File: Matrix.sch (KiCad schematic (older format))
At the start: 178 parts

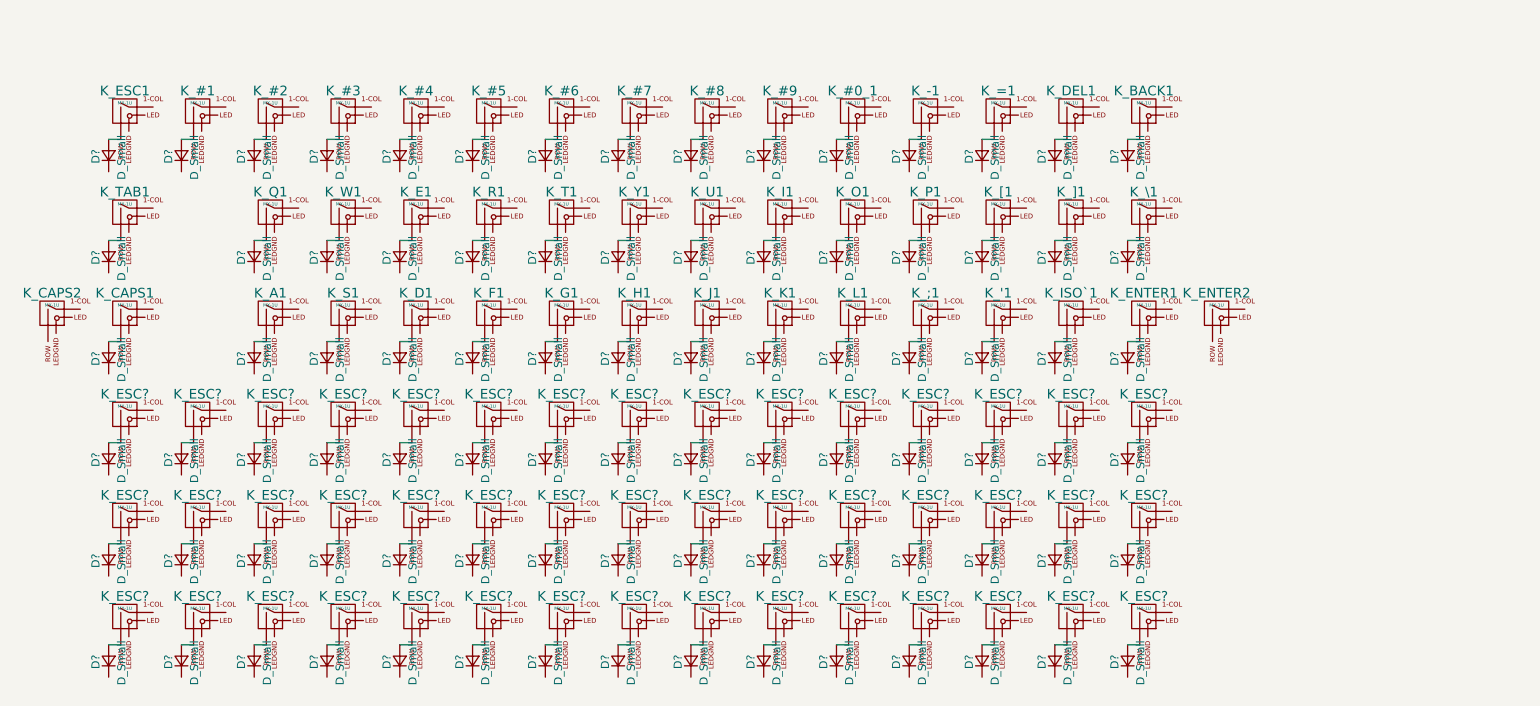
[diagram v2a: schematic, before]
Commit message: Build right shift in separate sheet
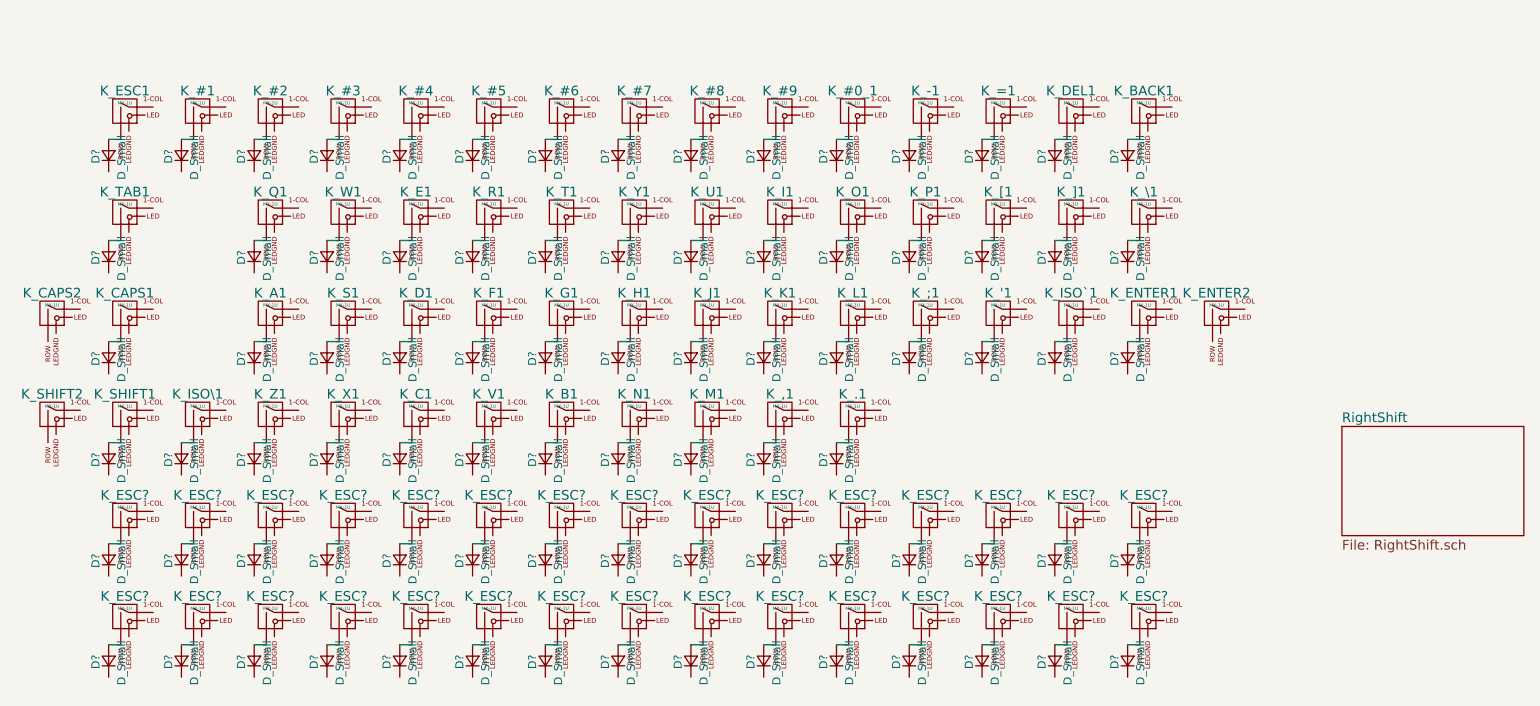
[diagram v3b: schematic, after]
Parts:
- removed D? (x34): D_Small, symbol D_Small
- removed K_ESC? (x34): MX-1U, symbol MX-1U
- added D? (x30): D_Small, symbol D_Small
- added K_ESC? (x30), K_SHIFT2: MX-1U, symbol MX-1U
- gave numbers to parts that had none: 11
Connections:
- new net: D?.2 (A), K_ESC?.2 (ROW) (x30)

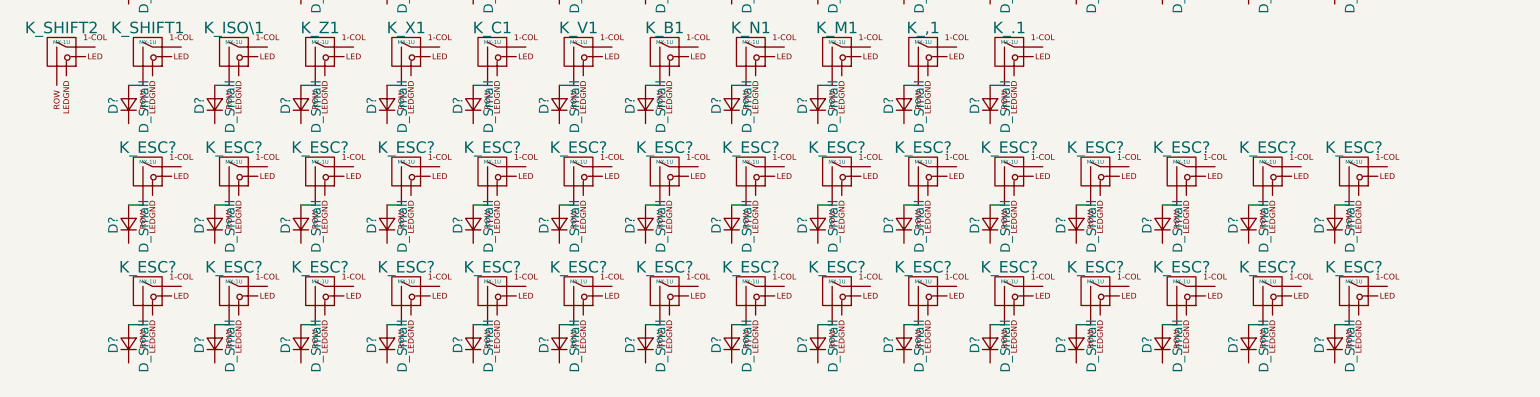
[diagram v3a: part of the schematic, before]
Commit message: Break matrix up into multiple sheets
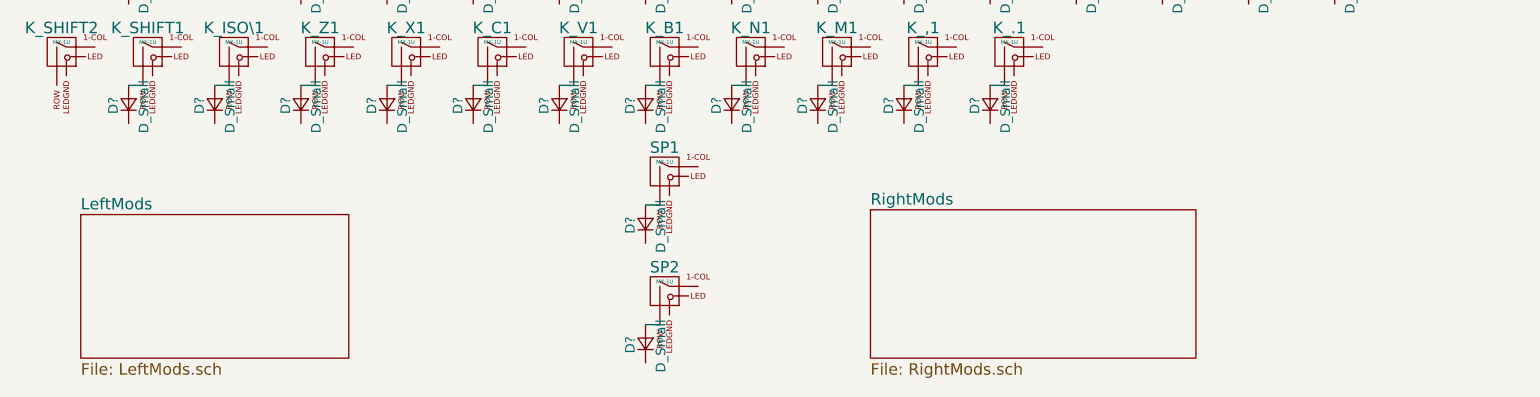
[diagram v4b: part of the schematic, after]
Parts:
- removed D? (x28): D_Small, symbol D_Small
- removed K_ESC? (x28): MX-1U, symbol MX-1U
- gave numbers to parts that had none: 2

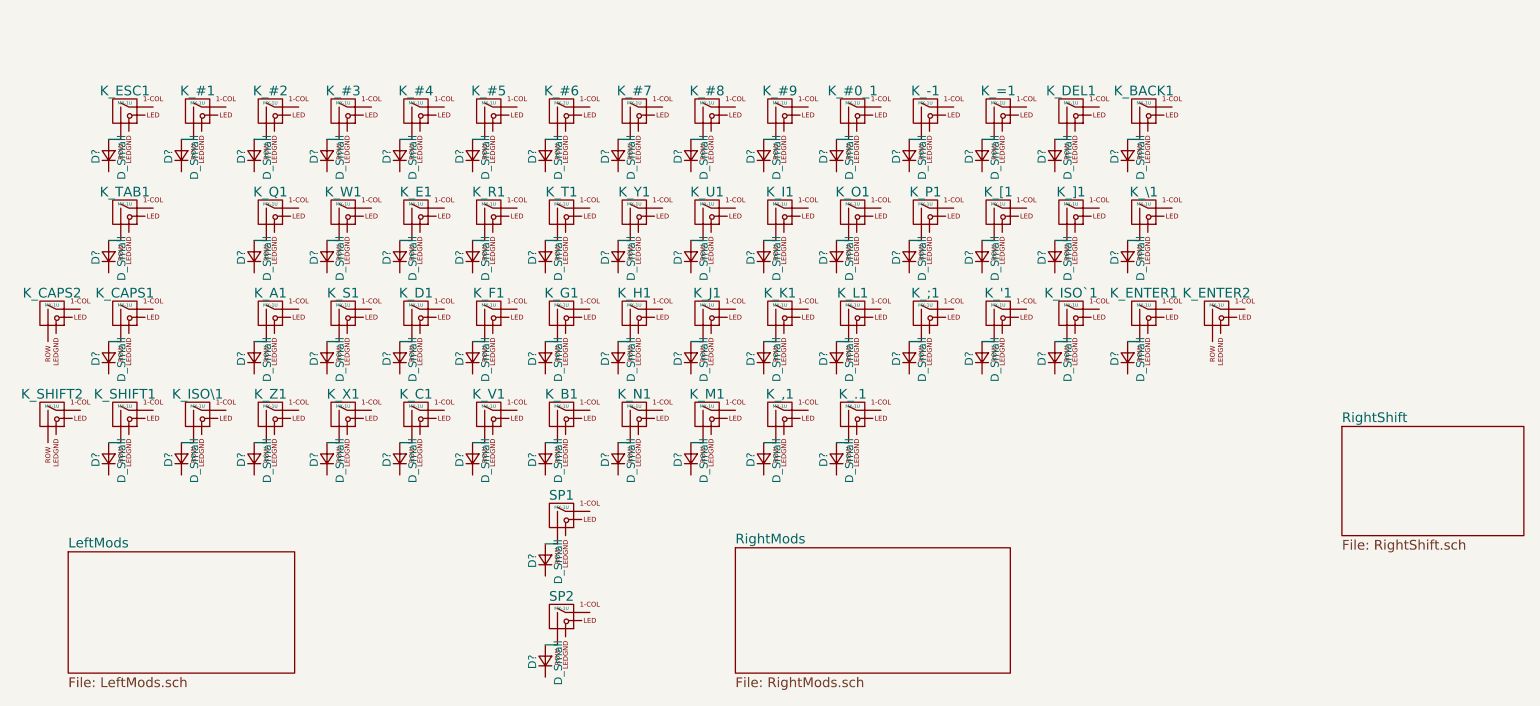
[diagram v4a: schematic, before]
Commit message: Assign footprints, along with placeholders for mx
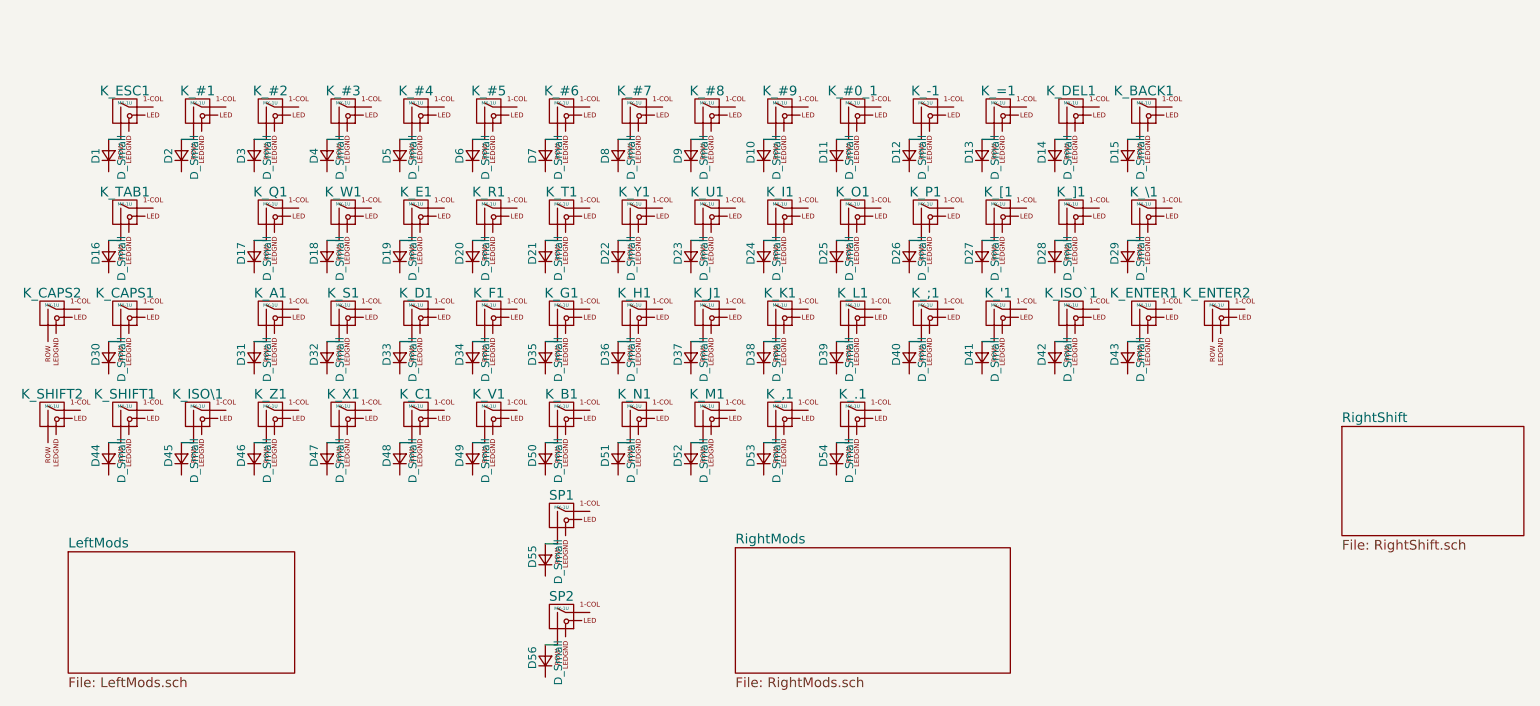
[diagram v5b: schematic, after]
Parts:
- D1, D10, D11, D12, D13, D14, D15, D16, D17, D18, D19, D2, D20, D21, D22, D23, D24, D25, D26, D27, D28, D29, D3, D30, D31, D32, D33, D34, D35, D36, D37, D38, D39, D4, D40, D41, D42, D43, D44, D45, D46, D47, D48, D49, D5, D50, D51, D52, D53, D54, D55, D56, D6, D7, D8, D9: renamed from D?; footprint (none) -> Diodes_SMD:D_SOD-123
- K_#0_1, K_#1, K_#2, K_#3, K_#4, K_#5, K_#6, K_#7, K_#8, K_#9, K_'1, K_,1, K_-1, K_.1, K_;1, K_=1, K_A1, K_B1, K_BACK1, K_C1, K_CAPS1, K_CAPS2, K_D1, K_DEL1, K_E1, K_ENTER1, K_ENTER2, K_ESC1, K_F1, K_G1, K_H1, K_I1, K_ISO\1, K_ISO`1, K_J1, K_K1, K_L1, K_M1, K_N1, K_O1, K_P1, K_Q1, K_R1, K_S1, K_SHIFT1, K_SHIFT2, K_T1, K_TAB1, K_U1, K_V1, K_W1, K_X1, K_Y1, K_Z1, K_[1, K_\1, K_]1, SP1, SP2: footprint (none) -> MX_Alps_Hybrid:MX-1U

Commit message: Repair footprints on main matrix sheet
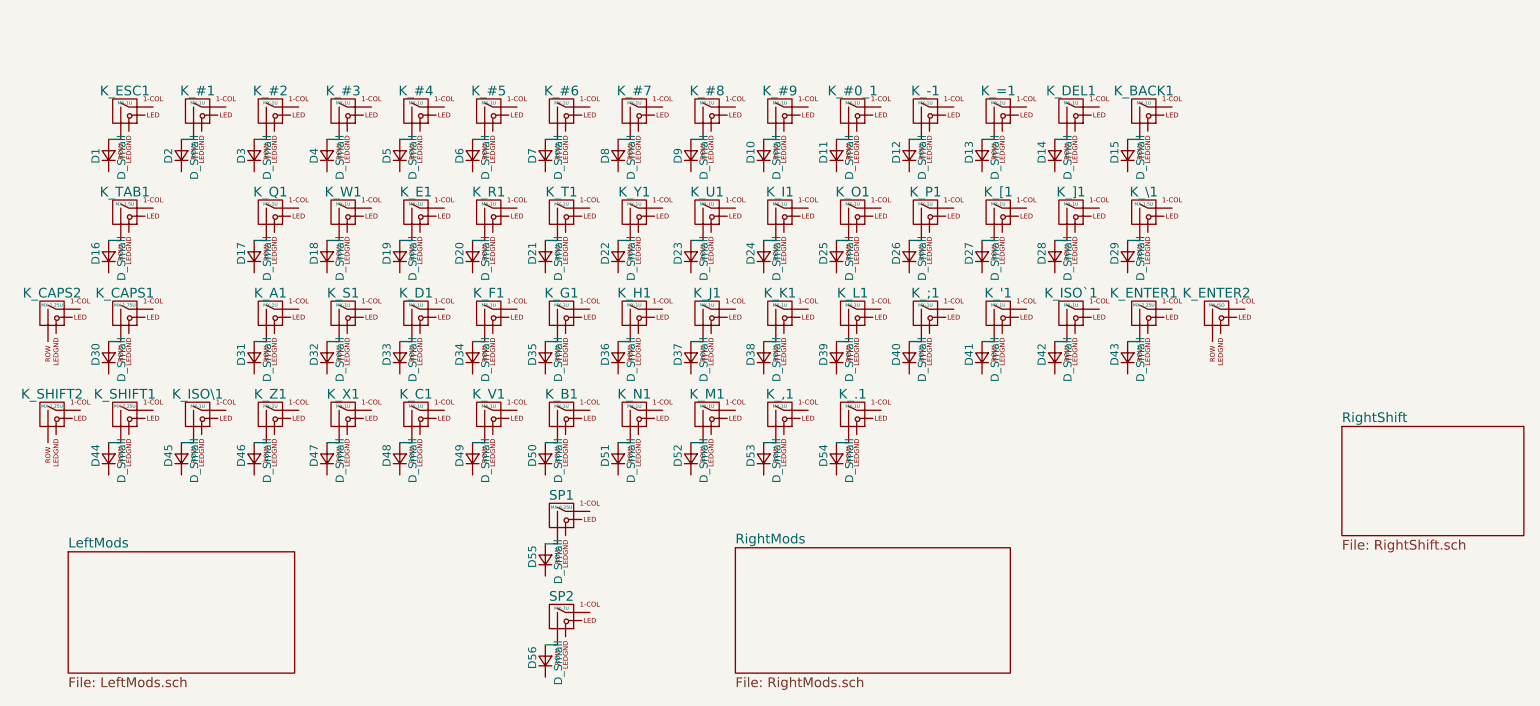
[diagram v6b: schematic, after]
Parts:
- K_CAPS1: value MX-1U -> MX-1.75U; footprint MX_Alps_Hybrid:MX-1U -> MX_Alps_Hybrid:MX-1.75U
- K_CAPS2, K_SHIFT2: value MX-1U -> MX-1.25U; footprint MX_Alps_Hybrid:MX-1U -> MX_Alps_Hybrid:MX-1.25U
- K_ENTER1, K_SHIFT1: value MX-1U -> MX-2.25U; footprint MX_Alps_Hybrid:MX-1U -> MX_Alps_Hybrid:MX-2.25U
- K_ENTER2: value MX-1U -> MX-ISO; footprint MX_Alps_Hybrid:MX-1U -> MX_Alps_Hybrid:MX-ISO-Combined-ReversedStabilizers
- K_TAB1, K_\1: value MX-1U -> MX-1.5U; footprint MX_Alps_Hybrid:MX-1U -> MX_Alps_Hybrid:MX-1.5U
- SP1: value MX-1U -> MX-6.25U; footprint MX_Alps_Hybrid:MX-1U -> MX_Alps_Hybrid:MX-6.25U-ReversedStabilizers
- SP2: value MX-1U -> MX-7U; footprint MX_Alps_Hybrid:MX-1U -> MX_Alps_Hybrid:MX-7U-ReversedStabilizers
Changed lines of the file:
@@
 P 1500 1850
 F 0 "K_TAB1" H 1500 1975 60  0000 C CNN
-F 1 "MX-1U" H 1500 1900 20  0000 C CNN
-F 2 "MX_Alps_Hybrid:MX-1U" H 1475 1825 60  0001 C CNN
+F 1 "MX-1.5U" H 1500 1900 20  0000 C CNN
+F 2 "MX_Alps_Hybrid:MX-1.5U" H 1475 1825 60  0001 C CNN
 F 3 "" H 1475 1825 60  0001 C CNN
 	1    1500 1850
@@
 P 7800 1850
 F 0 "K_\\1" H 7800 1975 60  0000 C CNN
-F 1 "MX-1U" H 7800 1900 20  0000 C CNN
-F 2 "MX_Alps_Hybrid:MX-1U" H 7775 1825 60  0001 C CNN
+F 1 "MX-1.5U" H 7800 1900 20  0000 C CNN
+F 2 "MX_Alps_Hybrid:MX-1.5U" H 7775 1825 60  0001 C CNN
 F 3 "" H 7775 1825 60  0001 C CNN
 	1    7800 1850
@@
 P 1500 2475
 F 0 "K_CAPS1" H 1500 2600 60  0000 C CNN
-F 1 "MX-1U" H 1500 2525 20  0000 C CNN
-F 2 "MX_Alps_Hybrid:MX-1U" H 1475 2450 60  0001 C CNN
+F 1 "MX-1.75U" H 1500 2525 20  0000 C CNN
+F 2 "MX_Alps_Hybrid:MX-1.75U" H 1475 2450 60  0001 C CNN
 F 3 "" H 1475 2450 60  0001 C CNN
 	1    1500 2475
@@
 P 7800 2475
 F 0 "K_ENTER1" H 7800 2600 60  0000 C CNN
-F 1 "MX-1U" H 7800 2525 20  0000 C CNN
-F 2 "MX_Alps_Hybrid:MX-1U" H 7775 2450 60  0001 C CNN
+F 1 "MX-2.25U" H 7800 2525 20  0000 C CNN
+F 2 "MX_Alps_Hybrid:MX-2.25U" H 7775 2450 60  0001 C CNN
 F 3 "" H 7775 2450 60  0001 C CNN
 	1    7800 2475
@@
 P 1500 3100
 F 0 "K_SHIFT1" H 1500 3225 60  0000 C CNN
-F 1 "MX-1U" H 1500 3150 20  0000 C CNN
-F 2 "MX_Alps_Hybrid:MX-1U" H 1475 3075 60  0001 C CNN
+F 1 "MX-2.25U" H 1500 3150 20  0000 C CNN
+F 2 "MX_Alps_Hybrid:MX-2.25U" H 1475 3075 60  0001 C CNN
 F 3 "" H 1475 3075 60  0001 C CNN
 	1    1500 3100
@@
 P 1050 2475
 F 0 "K_CAPS2" H 1050 2600 60  0000 C CNN
-F 1 "MX-1U" H 1050 2525 20  0000 C CNN
-F 2 "MX_Alps_Hybrid:MX-1U" H 1025 2450 60  0001 C CNN
+F 1 "MX-1.25U" H 1050 2525 20  0000 C CNN
+F 2 "MX_Alps_Hybrid:MX-1.25U" H 1025 2450 60  0001 C CNN
 F 3 "" H 1025 2450 60  0001 C CNN
 	1    1050 2475
@@
 P 8250 2475
 F 0 "K_ENTER2" H 8250 2600 60  0000 C CNN
-F 1 "MX-1U" H 8250 2525 20  0000 C CNN
-F 2 "MX_Alps_Hybrid:MX-1U" H 8225 2450 60  0001 C CNN
+F 1 "MX-ISO" H 8250 2525 20  0000 C CNN
+F 2 "MX_Alps_Hybrid:MX-ISO-Combined-ReversedStabilizers" H 8225 2450 60  0001 C CNN
 F 3 "" H 8225 2450 60  0001 C CNN
 	1    8250 2475
@@
 P 1050 3100
 F 0 "K_SHIFT2" H 1050 3225 60  0000 C CNN
-F 1 "MX-1U" H 1050 3150 20  0000 C CNN
-F 2 "MX_Alps_Hybrid:MX-1U" H 1025 3075 60  0001 C CNN
+F 1 "MX-1.25U" H 1050 3150 20  0000 C CNN
+F 2 "MX_Alps_Hybrid:MX-1.25U" H 1025 3075 60  0001 C CNN
 F 3 "" H 1025 3075 60  0001 C CNN
 	1    1050 3100
@@
 P 4200 3725
 F 0 "SP1" H 4200 3850 60  0000 C CNN
-F 1 "MX-1U" H 4200 3775 20  0000 C CNN
-F 2 "MX_Alps_Hybrid:MX-1U" H 4175 3700 60  0001 C CNN
+F 1 "MX-6.25U" H 4200 3775 20  0000 C CNN
+F 2 "MX_Alps_Hybrid:MX-6.25U-ReversedStabilizers" H 4175 3700 60  0001 C CNN
 F 3 "" H 4175 3700 60  0001 C CNN
 	1    4200 3725
@@
 P 4200 4350
 F 0 "SP2" H 4200 4475 60  0000 C CNN
-F 1 "MX-1U" H 4200 4400 20  0000 C CNN
-F 2 "MX_Alps_Hybrid:MX-1U" H 4175 4325 60  0001 C CNN
+F 1 "MX-7U" H 4200 4400 20  0000 C CNN
+F 2 "MX_Alps_Hybrid:MX-7U-ReversedStabilizers" H 4175 4325 60  0001 C CNN
 F 3 "" H 4175 4325 60  0001 C CNN
 	1    4200 4350

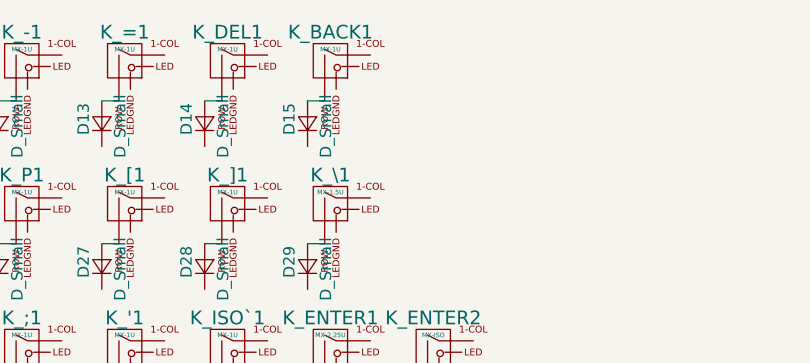
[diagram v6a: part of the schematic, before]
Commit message: Fix backspace, finish row 1
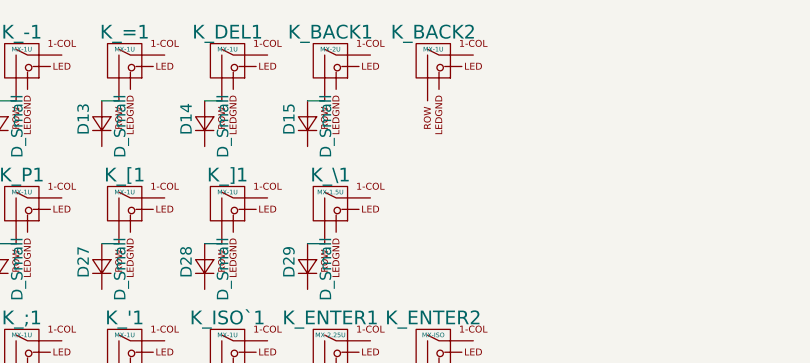
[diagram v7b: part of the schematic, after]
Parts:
- added K_BACK2: MX-1U, MX_Alps_Hybrid:MX-1U, symbol MX-1U
- K_BACK1: value MX-1U -> MX-2U; footprint MX_Alps_Hybrid:MX-1U -> MX_Alps_Hybrid:MX-2U
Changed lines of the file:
@@
 P 7800 1225
 F 0 "K_BACK1" H 7800 1350 60  0000 C CNN
-F 1 "MX-1U" H 7800 1275 20  0000 C CNN
-F 2 "MX_Alps_Hybrid:MX-1U" H 7775 1200 60  0001 C CNN
+F 1 "MX-2U" H 7800 1275 20  0000 C CNN
+F 2 "MX_Alps_Hybrid:MX-2U" H 7775 1200 60  0001 C CNN
 F 3 "" H 7775 1200 60  0001 C CNN
 	1    7800 1225
@@
 F1 "RightMods.sch" 60
 $EndSheet
+$Comp
+L MX-1U K_BACK2
+U 1 1 5A6A6B25
+P 8250 1225
+F 0 "K_BACK2" H 8250 1350 60  0000 C CNN
+F 1 "MX-1U" H 8250 1275 20  0000 C CNN
+F 2 "MX_Alps_Hybrid:MX-1U" H 8225 1200 60  0001 C CNN
+F 3 "" H 8225 1200 60  0001 C CNN
+	1    8250 1225
+	1    0    0    -1
+$EndComp
 $EndSCHEMATC
